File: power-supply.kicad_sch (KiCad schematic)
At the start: 41 parts, among them J2 USB_C_Receptacle_USB2.0, J3 Conn_01x02_Female, Q1 AO3401A, Q2 AO3401A, Q3 AO3401A, Q4 BC817, Q5 BC817, Q6 BC817, U101 AMS1117-3.3, U102 LTC4412, U103 LTC4412, U104 LTC4412

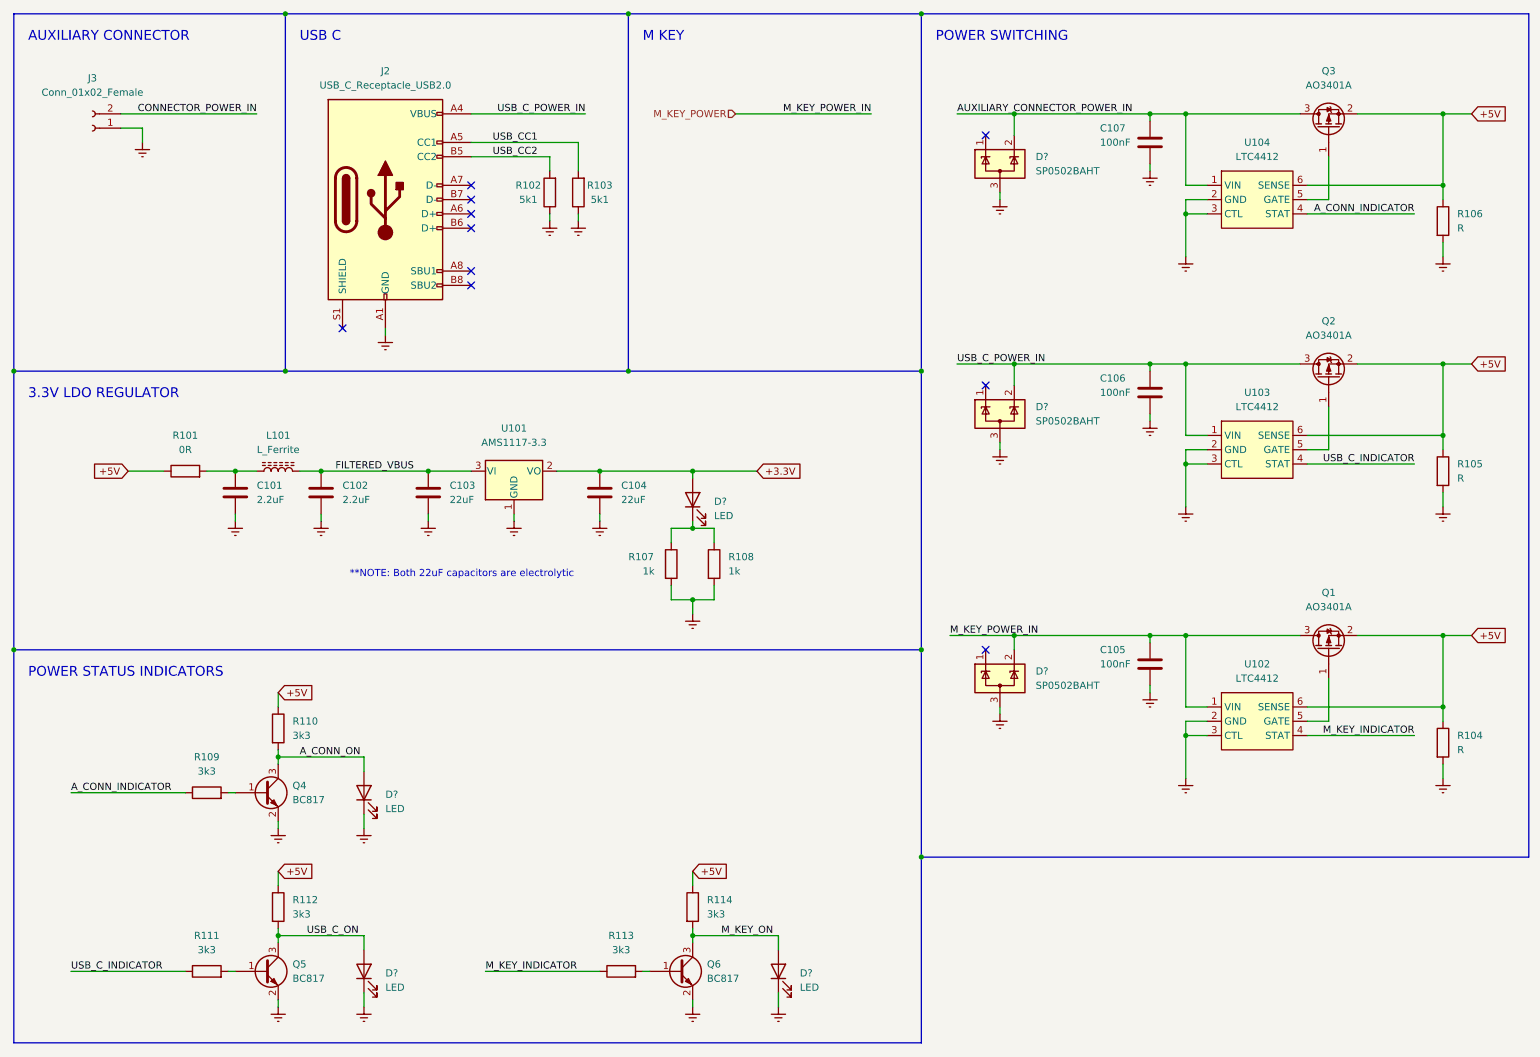
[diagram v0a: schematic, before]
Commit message: updated bus aliases; added resistor values to RF section; added component to Fruitly_RF library
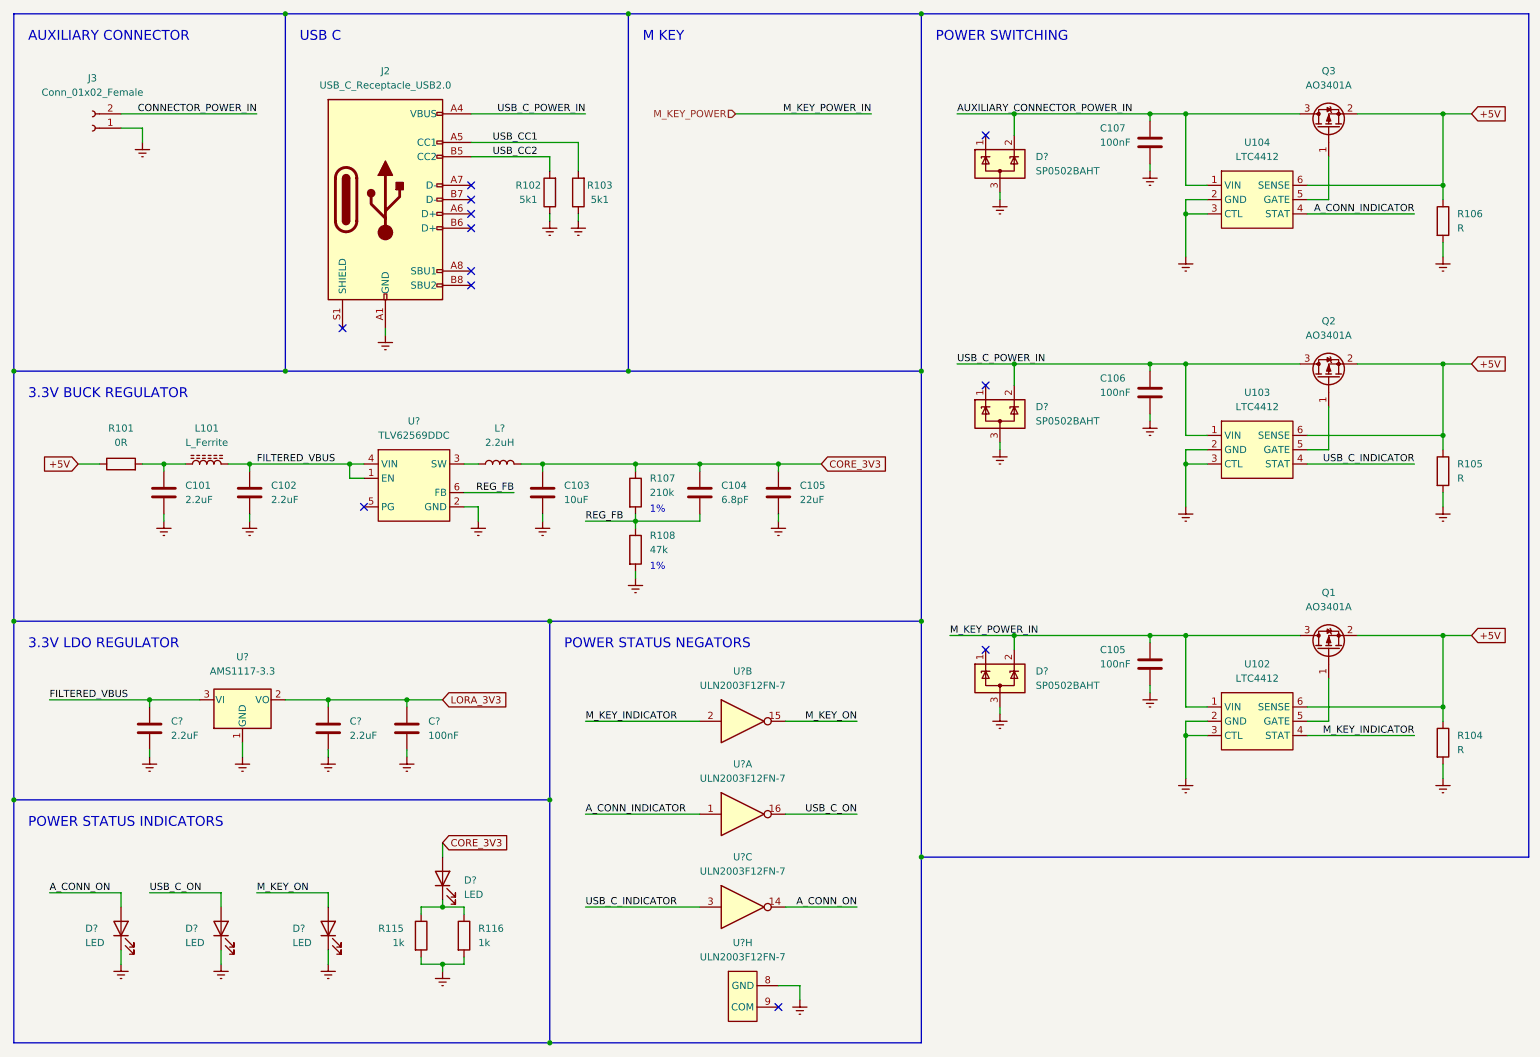
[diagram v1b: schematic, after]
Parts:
- removed D? (x4): LED, LED_SMD:LED_0603_1608Metric, symbol Device:LED
- removed Q4, Q5, Q6: BC817, Package_TO_SOT_SMD:SOT-23, symbol Transistor_BJT:BC817
- removed R109, R111, R113: 3k3, Capacitor_SMD:C_0402_1005Metric, symbol Device:R
- removed R110, R112, R114: 3k3, Capacitor_SMD:C_0603_1608Metric, symbol Device:R
- removed U101: AMS1117-3.3, Package_TO_SOT_SMD:SOT-223-3_TabPin2, symbol Regulator_Linear:AMS1117-3.3
- added C105: 22uF, Capacitor_SMD:C_0805_2012Metric, symbol Device:C
- added C? (x2): 2.2uF, Capacitor_SMD:C_0805_2012Metric, symbol Device:C
- added C?: 100nF, Capacitor_SMD:C_0805_2012Metric, symbol Device:C
- added D? (x4): LED, LED_SMD:LED_0603_1608Metric, symbol Device:LED
- added L?: 2.2uH, symbol Device:L
- added R115, R116: 1k, Resistor_SMD:R_0603_1608Metric, symbol Device:R
- added U? (x4): ULN2003F12FN-7, symbol Fruitfly_Logic:ULN2003F12FN-7
- added U?: AMS1117-3.3, Package_TO_SOT_SMD:SOT-223-3_TabPin2, symbol Regulator_Linear:AMS1117-3.3
- added U?: TLV62569DDC, symbol Fruitfly_Power:TLV62569DDC
- C103: value 22uF -> 10uF
- C104: value 22uF -> 6.8pF; footprint Capacitor_SMD:C_0805_2012Metric -> Capacitor_SMD:C_0603_1608Metric
- R107: value 1k -> 210k
- R108: value 1k -> 47k
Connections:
- net +3.3V is gone; now on net CORE_3V3: C104.1
- net A_CONN_INDICATOR: now also U?.1
- net A_CONN_ON: now also D?.2 (A), U?.14
- net Earth: now also C105.2, C?.2, C?.2, C?.2, D?.1 (K), D?.1 (K), D?.1 (K), R115.2, R116.2, U?.1 (GND), U?.2 (GND), U?.8 (GND); no longer C104.2, R107.2
- net FILTERED_VBUS: now also C?.1, U?.1 (EN), U?.3 (VI), U?.4 (VIN); no longer C103.1
- net M_KEY_INDICATOR: now also U?.2
- net M_KEY_ON: now also D?.2 (A), U?.15
- net USB_C_INDICATOR: now also U?.3
- net USB_C_ON: now also D?.2 (A), U?.16
- net CORE_3V3: now reaches R107.1
- net CORE_3V3: now also C103.1, C105.1, D?.2 (A), L?.2; no longer R108.1
- new net: D?.1 (K), R115.1, R116.1
- new net: L?.1, U?.3 (SW)
- new net LORA_3V3: C?.1, C?.1, U?.2 (VO)
- new net REG_FB: C104.2, R107.2, R108.1, U?.6 (FB)
- no-connect marks 10 -> 12
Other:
- note added: "1%"
- note added: "3.3V BUCK REGULATOR"
- note added: "POWER STATUS NEGATORS"
- note removed: "**NOTE: Both 22uF capacitors are electrolytic"
- moved on the sheet: C101, C102, L101, R101
